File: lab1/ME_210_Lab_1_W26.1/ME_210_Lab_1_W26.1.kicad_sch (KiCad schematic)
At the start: 5 parts, among them Q1 BPW40, U1 ${SIM.PARAMS}

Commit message: lab 1 p5 done
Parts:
- added D1, D2: LED, symbol Device:LED
- added Q2, Q3, Q4: BPW40, LED_THT:LED_D5.0mm_Clear, symbol Sensor_Optical:BPW40
- added R10: 2k, symbol Device:R
- added R11, R4, R6: 1k, symbol Device:R
- added R12, R8: 5k, symbol Device:R
- added R13: 3k3, symbol Device:R
- added R14: 47k, symbol Device:R
- added R5, R7: 250, symbol Device:R
- added R9: 220, symbol Device:R
- added U2: ${SIM.PARAMS}, symbol Simulation_SPICE:OPAMP
- added U3: LM339, Package_TO_SOT_SMD:SOT-23-5, symbol Comparator:LM397
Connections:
- net +5V: now also D1.2 (A), D2.2 (A), Q2.1 (C), Q4.1 (C), R13.2, R6.2, R8.2, U2.3 (V+), U3.5 (V+)
- net GND: now also Q3.2 (E), R11.1, R12.1, R4.1, R5.1, R7.1, R9.1, U2.4 (V-), U3.2 (V-)
- new net: R10.1, R9.2, U2.2 (-)
- new net: D1.1 (K), R5.2
- new net: R12.2, R14.2, R8.1, U3.3 (+)
- new net: R13.1, R14.1, U3.4
- new net: D2.1 (K), R7.2
- new net Vout: Q2.2 (E), Q3.1 (C), R10.2, R4.2, R6.1, U2.5
- new net Vsig: Q4.2 (E), R11.2, U2.1 (+), U3.1 (-)
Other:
- note added: "Q2.2"
- note added: "Q2.5"
- note added: "Q3.1"
- note added: "Q4"
- note added: "Q5.2"
- moved on the sheet: Q1, R1, R2, R3, U1

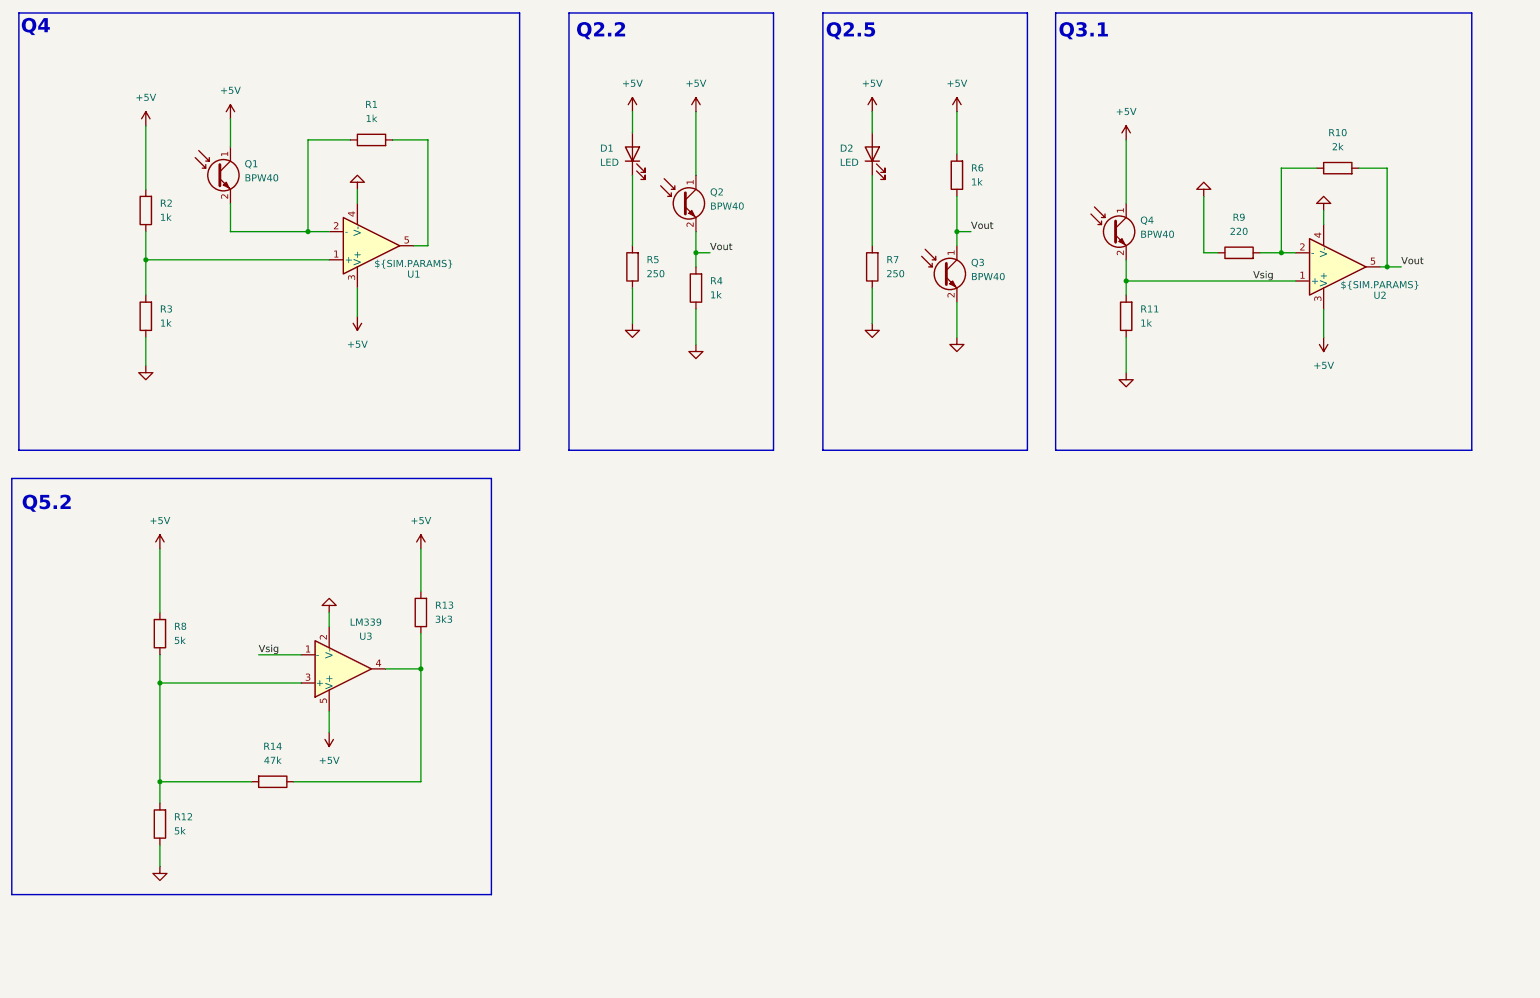
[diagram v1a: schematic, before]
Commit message: added lab report template for lab2
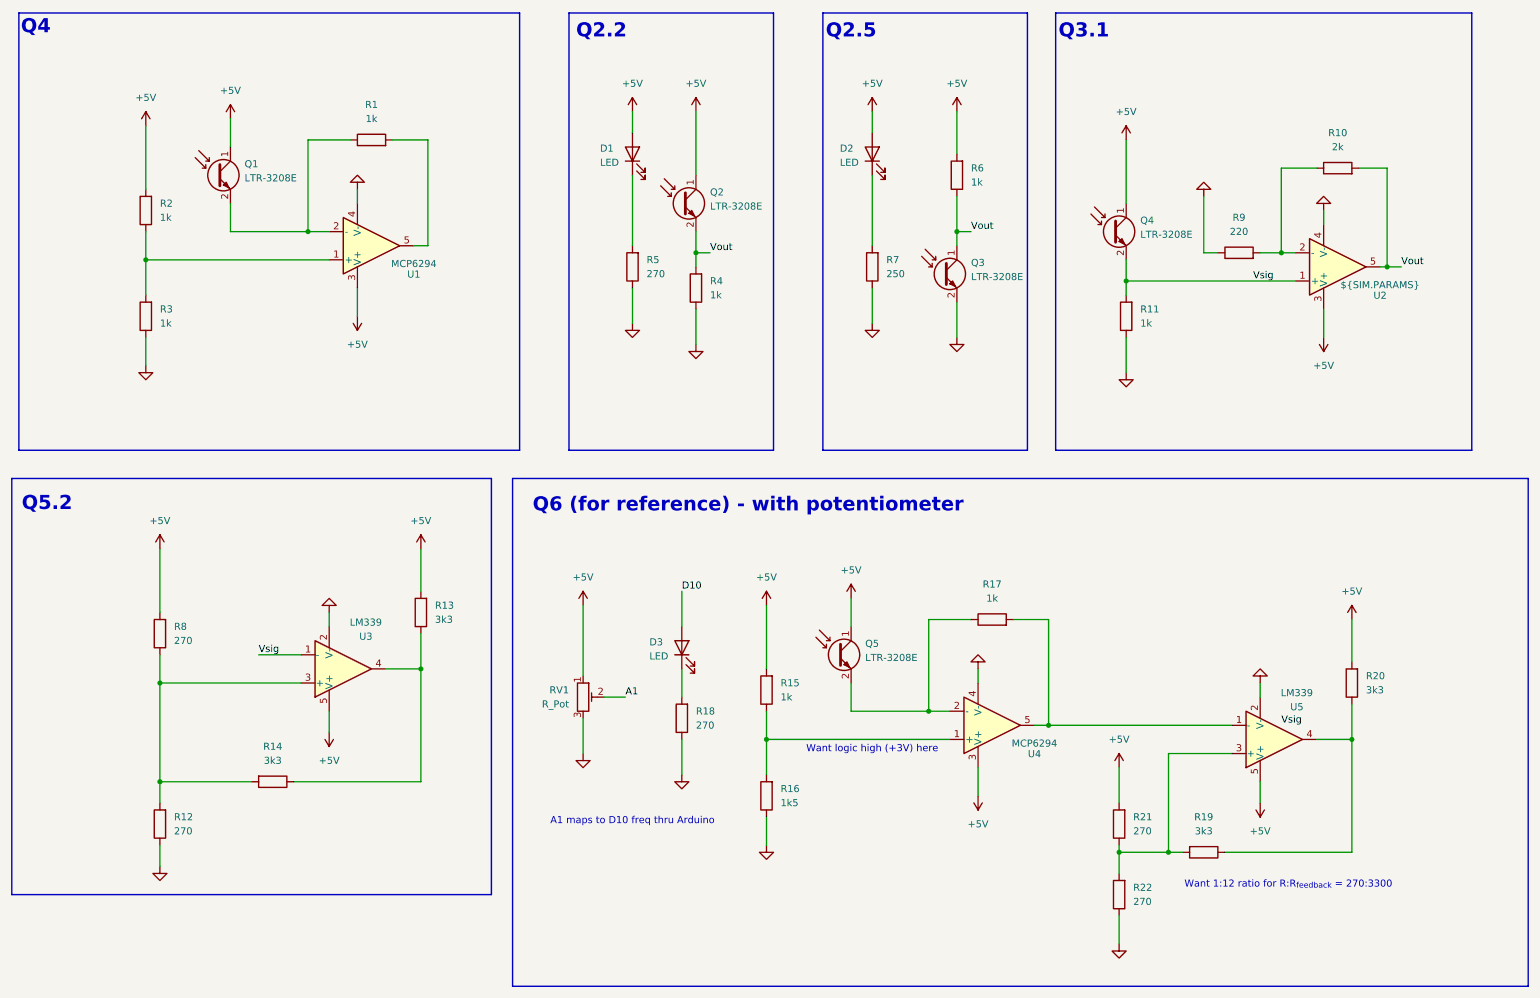
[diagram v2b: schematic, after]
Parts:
- added D3: LED, symbol Device:LED
- added Q5: LTR-3208E, LED_THT:LED_D5.0mm_Clear, symbol Sensor_Optical:BPW40
- added R15, R17: 1k, symbol Device:R
- added R16: 1k5, symbol Device:R
- added R18, R21, R22: 270, symbol Device:R
- added R19, R20: 3k3, symbol Device:R
- added RV1: R_Pot, symbol Device:R_Potentiometer_Trim
- added U4: MCP6294, symbol Simulation_SPICE:OPAMP
- added U5: LM339, Package_TO_SOT_SMD:SOT-23-5, symbol Comparator:LM397
- Q1, Q2, Q3, Q4: value BPW40 -> LTR-3208E
- R12, R8: value 5k -> 270
- R14: value 47k -> 3k3
- R5: value 250 -> 270
- U1: value ${SIM.PARAMS} -> MCP6294
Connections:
- net +5V: now also Q5.1 (C), R15.2, R20.2, R21.2, RV1.1, U4.3 (V+), U5.5 (V+)
- net GND: now also R16.1, R18.1, R22.1, RV1.3, U4.4 (V-), U5.2 (V-)
- new net: R19.1, R20.1, U5.4
- new net: R19.2, R21.1, R22.2, U5.3 (+)
- new net: Q5.2 (E), R17.1, U4.2 (-)
- new net: R17.2, U4.5, U5.1 (-)
- new net: R15.1, R16.2, U4.1 (+)
- new net: D3.1 (K), R18.2
- new net A1: RV1.2
- new net D10: D3.2 (A)
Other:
- note added: "A1 maps to D10 freq thru Arduino"
- note added: "Q6 (for reference) - with potentiometer"
- note added: "Want 1:12 ratio for R:R_{feedback} = 270:3300"
- note added: "Want logic high (+3V) here"
